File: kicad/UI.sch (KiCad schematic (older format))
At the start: 14 parts, among them Q14 DMN3065LW-7, SW2 UPLOAD, U8 PCA9632

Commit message: コンデンサを追加
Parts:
- renumbered C16 to C17
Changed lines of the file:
@@
 $EndDescr
 $Comp
-L power:GND #PWR070
+L power:GND #PWR072
 U 1 1 57CEA2EF
 P 6500 4600
-F 0 "#PWR070" H 6500 4350 50  0001 C CNN
+F 0 "#PWR072" H 6500 4350 50  0001 C CNN
 F 1 "GND" H 6500 4450 50  0000 C CNN
 F 2 "" H 6500 4600 50  0000 C CNN
@@
 	6500 4600 6500 4400
 $Comp
-L power:GND #PWR072
+L power:GND #PWR074
 U 1 1 5A1C53C4
 P 7900 4600
-F 0 "#PWR072" H 7900 4350 50  0001 C CNN
+F 0 "#PWR074" H 7900 4350 50  0001 C CNN
 F 1 "GND" H 7900 4450 50  0000 C CNN
 F 2 "" H 7900 4600 50  0000 C CNN
@@
 SDA
 $Comp
-L power:+3.3V #PWR064
+L power:+3.3V #PWR066
 U 1 1 5A202D5A
 P 4050 3150
-F 0 "#PWR064" H 4050 3000 50  0001 C CNN
+F 0 "#PWR066" H 4050 3000 50  0001 C CNN
 F 1 "+3.3V" H 4050 3290 50  0000 C CNN
 F 2 "" H 4050 3150 50  0001 C CNN
@@
 	4050 3150 4050 3250
 $Comp
-L power:GND #PWR065
+L power:GND #PWR067
 U 1 1 5A202F53
 P 4050 4650
-F 0 "#PWR065" H 4050 4400 50  0001 C CNN
+F 0 "#PWR067" H 4050 4400 50  0001 C CNN
 F 1 "GND" H 4050 4500 50  0000 C CNN
 F 2 "" H 4050 4650 50  0000 C CNN
@@
 	5050 3450 5050 3550
 $Comp
-L power:+3.3V #PWR067
+L power:+3.3V #PWR069
 U 1 1 5A204571
 P 5050 3150
-F 0 "#PWR067" H 5050 3000 50  0001 C CNN
+F 0 "#PWR069" H 5050 3000 50  0001 C CNN
 F 1 "+3.3V" H 5050 3290 50  0000 C CNN
 F 2 "" H 5050 3150 50  0001 C CNN
@@
 	4750 3450 4750 3550
 $Comp
-L power:+3.3V #PWR066
+L power:+3.3V #PWR068
 U 1 1 5A203D72
 P 4750 3150
-F 0 "#PWR066" H 4750 3000 50  0001 C CNN
+F 0 "#PWR068" H 4750 3000 50  0001 C CNN
 F 1 "+3.3V" H 4750 3290 50  0000 C CNN
 F 2 "" H 4750 3150 50  0001 C CNN
@@
 	5650 3450 5650 3550
 $Comp
-L power:+3.3V #PWR069
+L power:+3.3V #PWR071
 U 1 1 5A20460C
 P 5650 3150
-F 0 "#PWR069" H 5650 3000 50  0001 C CNN
+F 0 "#PWR071" H 5650 3000 50  0001 C CNN
 F 1 "+3.3V" H 5650 3290 50  0000 C CNN
 F 2 "" H 5650 3150 50  0001 C CNN
@@
 	5350 3450 5350 3550
 $Comp
-L power:+3.3V #PWR068
+L power:+3.3V #PWR070
 U 1 1 5A204620
 P 5350 3150
-F 0 "#PWR068" H 5350 3000 50  0001 C CNN
+F 0 "#PWR070" H 5350 3000 50  0001 C CNN
 F 1 "+3.3V" H 5350 3290 50  0000 C CNN
 F 2 "" H 5350 3150 50  0001 C CNN
@@
 	5650 4250 5650 3850
 $Comp
-L Device:C_Small C16
+L Device:C_Small C17
 U 1 1 5A2A1F42
 P 3850 3450
-F 0 "C16" H 3860 3520 50  0000 L CNN
+F 0 "C17" H 3860 3520 50  0000 L CNN
 F 1 "0.1u" H 3860 3370 50  0000 L CNN
 F 2 "Capacitors_SMD:C_0201_NoSilk" H 3850 3450 50  0001 C CNN
@@
 $EndComp
 $Comp
-L power:GND #PWR063
+L power:GND #PWR065
 U 1 1 5A2A2041
 P 3850 3550
-F 0 "#PWR063" H 3850 3300 50  0001 C CNN
+F 0 "#PWR065" H 3850 3300 50  0001 C CNN
 F 1 "GND" H 3850 3400 50  0000 C CNN
 F 2 "" H 3850 3550 50  0001 C CNN
@@
 	7500 4300 7600 4300
 $Comp
-L power:+3.3V #PWR071
+L power:+3.3V #PWR073
 U 1 1 5B6724D4
 P 7900 3400
-F 0 "#PWR071" H 7900 3250 50  0001 C CNN
+F 0 "#PWR073" H 7900 3250 50  0001 C CNN
 F 1 "+3.3V" H 7900 3540 50  0000 C CNN
 F 2 "" H 7900 3400 50  0001 C CNN

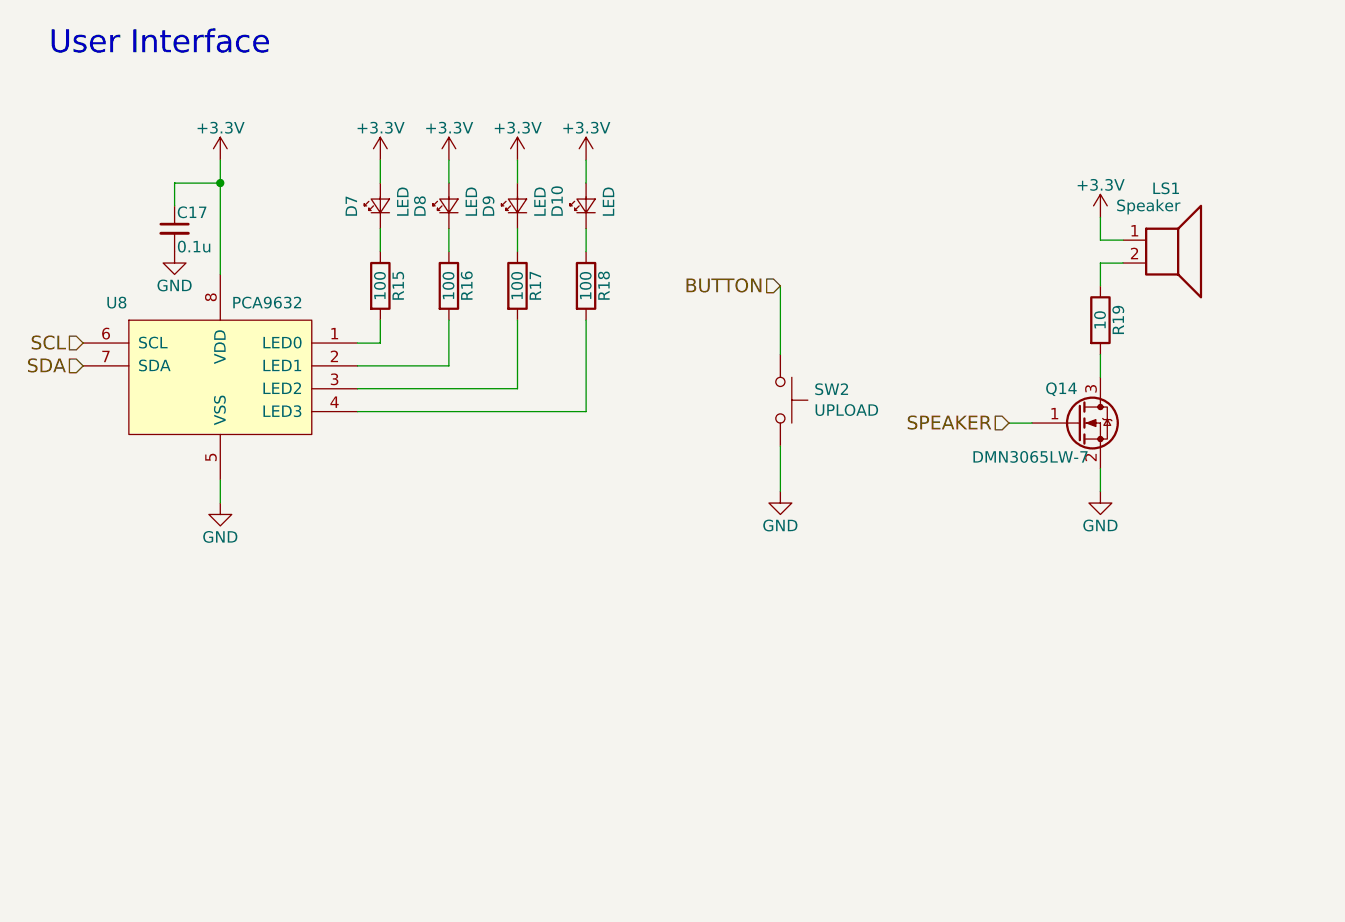
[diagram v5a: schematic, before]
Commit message: KERISEv4-5に向けて回路図を更新
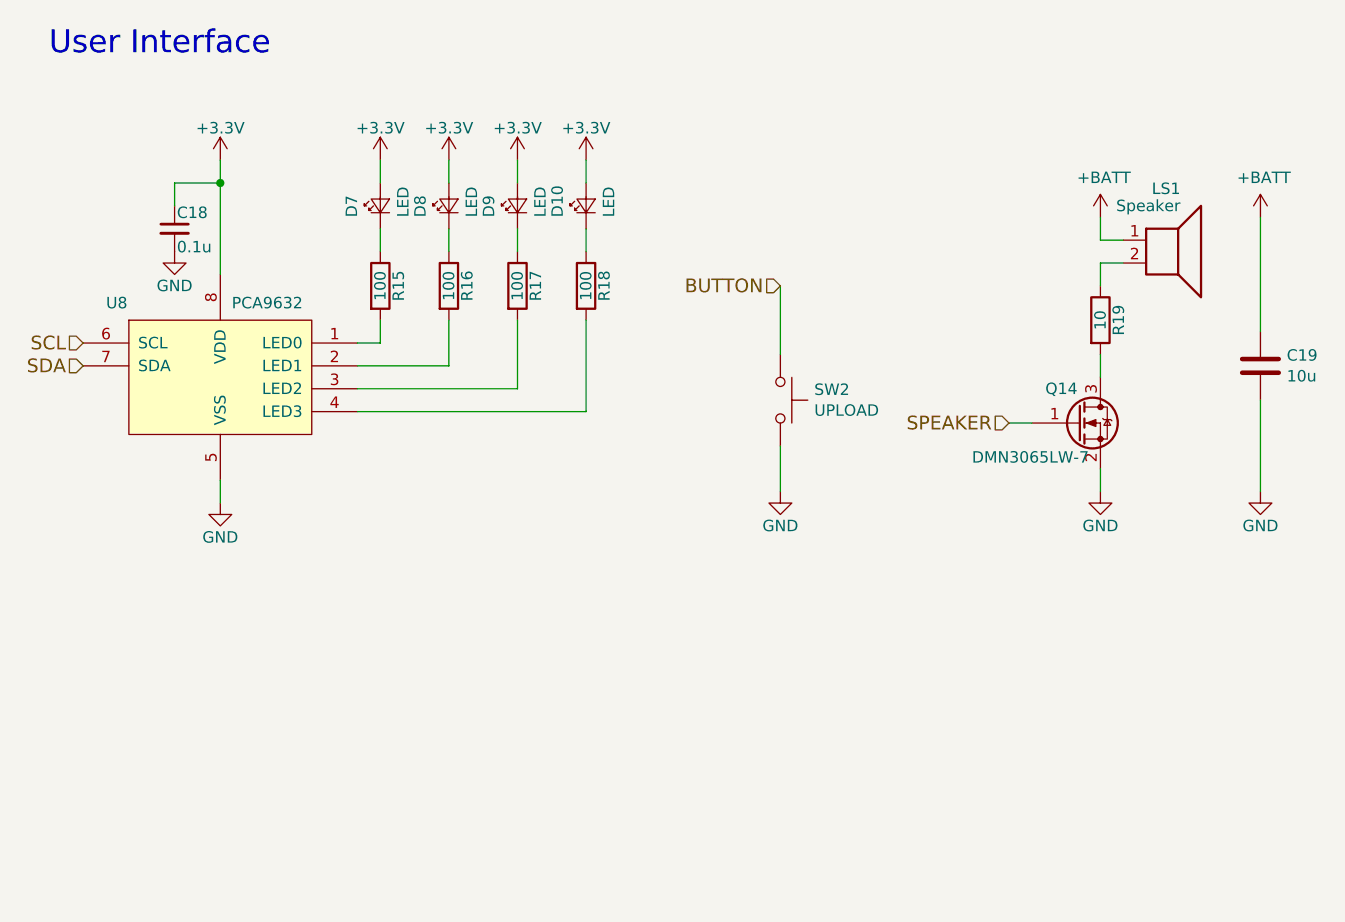
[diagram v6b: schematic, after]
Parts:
- added C19: 10u, symbol Device:C
- renumbered C17 to C18
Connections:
- net +3V3: no longer LS1.1
- net GND: now also C19.2
- new net +BATT: C19.1, LS1.1
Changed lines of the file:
@@
 $Descr A4 11693 8268
 encoding utf-8
-Sheet 14 14
+Sheet 14 15
 Title ""
 Date ""
@@
 $EndDescr
 $Comp
-L power:GND #PWR072
+L power:GND #PWR074
 U 1 1 57CEA2EF
 P 6500 4600
-F 0 "#PWR072" H 6500 4350 50  0001 C CNN
+F 0 "#PWR074" H 6500 4350 50  0001 C CNN
 F 1 "GND" H 6500 4450 50  0000 C CNN
 F 2 "" H 6500 4600 50  0000 C CNN
@@
 	6500 4600 6500 4400
 $Comp
-L power:GND #PWR074
+L power:GND #PWR076
 U 1 1 5A1C53C4
 P 7900 4600
-F 0 "#PWR074" H 7900 4350 50  0001 C CNN
+F 0 "#PWR076" H 7900 4350 50  0001 C CNN
 F 1 "GND" H 7900 4450 50  0000 C CNN
 F 2 "" H 7900 4600 50  0000 C CNN
@@
 SDA
 $Comp
-L power:+3.3V #PWR066
+L power:+3.3V #PWR068
 U 1 1 5A202D5A
 P 4050 3150
-F 0 "#PWR066" H 4050 3000 50  0001 C CNN
+F 0 "#PWR068" H 4050 3000 50  0001 C CNN
 F 1 "+3.3V" H 4050 3290 50  0000 C CNN
 F 2 "" H 4050 3150 50  0001 C CNN
@@
 	4050 3150 4050 3250
 $Comp
-L power:GND #PWR067
+L power:GND #PWR069
 U 1 1 5A202F53
 P 4050 4650
-F 0 "#PWR067" H 4050 4400 50  0001 C CNN
+F 0 "#PWR069" H 4050 4400 50  0001 C CNN
 F 1 "GND" H 4050 4500 50  0000 C CNN
 F 2 "" H 4050 4650 50  0000 C CNN
@@
 	5050 3450 5050 3550
 $Comp
-L power:+3.3V #PWR069
+L power:+3.3V #PWR071
 U 1 1 5A204571
 P 5050 3150
-F 0 "#PWR069" H 5050 3000 50  0001 C CNN
+F 0 "#PWR071" H 5050 3000 50  0001 C CNN
 F 1 "+3.3V" H 5050 3290 50  0000 C CNN
 F 2 "" H 5050 3150 50  0001 C CNN
@@
 	4750 3450 4750 3550
 $Comp
-L power:+3.3V #PWR068
+L power:+3.3V #PWR070
 U 1 1 5A203D72
 P 4750 3150
-F 0 "#PWR068" H 4750 3000 50  0001 C CNN
+F 0 "#PWR070" H 4750 3000 50  0001 C CNN
 F 1 "+3.3V" H 4750 3290 50  0000 C CNN
 F 2 "" H 4750 3150 50  0001 C CNN
@@
 	5650 3450 5650 3550
 $Comp
-L power:+3.3V #PWR071
+L power:+3.3V #PWR073
 U 1 1 5A20460C
 P 5650 3150
-F 0 "#PWR071" H 5650 3000 50  0001 C CNN
+F 0 "#PWR073" H 5650 3000 50  0001 C CNN
 F 1 "+3.3V" H 5650 3290 50  0000 C CNN
 F 2 "" H 5650 3150 50  0001 C CNN
@@
 	5350 3450 5350 3550
 $Comp
-L power:+3.3V #PWR070
+L power:+3.3V #PWR072
 U 1 1 5A204620
 P 5350 3150
-F 0 "#PWR070" H 5350 3000 50  0001 C CNN
+F 0 "#PWR072" H 5350 3000 50  0001 C CNN
 F 1 "+3.3V" H 5350 3290 50  0000 C CNN
 F 2 "" H 5350 3150 50  0001 C CNN
@@
 	5650 4250 5650 3850
 $Comp
-L Device:C_Small C17
+L Device:C_Small C18
 U 1 1 5A2A1F42
 P 3850 3450
-F 0 "C17" H 3860 3520 50  0000 L CNN
+F 0 "C18" H 3860 3520 50  0000 L CNN
 F 1 "0.1u" H 3860 3370 50  0000 L CNN
 F 2 "Capacitors_SMD:C_0201_NoSilk" H 3850 3450 50  0001 C CNN
@@
 $EndComp
 $Comp
-L power:GND #PWR065
+L power:GND #PWR067
 U 1 1 5A2A2041
 P 3850 3550
-F 0 "#PWR065" H 3850 3300 50  0001 C CNN
+F 0 "#PWR067" H 3850 3300 50  0001 C CNN
 F 1 "GND" H 3850 3400 50  0000 C CNN
 F 2 "" H 3850 3550 50  0001 C CNN
@@
 Wire Wire Line
 	7500 4300 7600 4300
-$Comp
-L power:+3.3V #PWR073
-U 1 1 5B6724D4
-P 7900 3400
-F 0 "#PWR073" H 7900 3250 50  0001 C CNN
-F 1 "+3.3V" H 7900 3540 50  0000 C CNN
-F 2 "" H 7900 3400 50  0001 C CNN
-F 3 "" H 7900 3400 50  0001 C CNN
-	1    7900 3400
-	1    0    0    -1
-$EndComp
 $Comp
 L Device:R R19
@@
 	0    1    1    0
 $EndComp
+$Comp
+L power:+BATT #PWR075
+U 1 1 5C29DB6A
+P 7900 3400
+F 0 "#PWR075" H 7900 3250 50  0001 C CNN
+F 1 "+BATT" H 7915 3573 50  0000 C CNN
+F 2 "" H 7900 3400 50  0001 C CNN
+F 3 "" H 7900 3400 50  0001 C CNN
+	1    7900 3400
+	1    0    0    -1
+$EndComp
+$Comp
+L Device:C C19
+U 1 1 5C29E0A6
+P 8600 4050
+F 0 "C19" H 8715 4096 50  0000 L CNN
+F 1 "10u" H 8715 4005 50  0000 L CNN
+F 2 "" H 8638 3900 50  0001 C CNN
+F 3 "~" H 8600 4050 50  0001 C CNN
+	1    8600 4050
+	1    0    0    -1
+$EndComp
+$Comp
+L power:+BATT #PWR077
+U 1 1 5C29E17B
+P 8600 3400
+F 0 "#PWR077" H 8600 3250 50  0001 C CNN
+F 1 "+BATT" H 8615 3573 50  0000 C CNN
+F 2 "" H 8600 3400 50  0001 C CNN
+F 3 "" H 8600 3400 50  0001 C CNN
+	1    8600 3400
+	1    0    0    -1
+$EndComp
+$Comp
+L power:GND #PWR078
+U 1 1 5C29E1A4
+P 8600 4600
+F 0 "#PWR078" H 8600 4350 50  0001 C CNN
+F 1 "GND" H 8600 4450 50  0000 C CNN
+F 2 "" H 8600 4600 50  0000 C CNN
+F 3 "" H 8600 4600 50  0000 C CNN
+	1    8600 4600
+	1    0    0    -1
+$EndComp
+Wire Wire Line
+	8600 4600 8600 4200
+Wire Wire Line
+	8600 3900 8600 3400
 $EndSCHEMATC

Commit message: フットプリントを割り当て
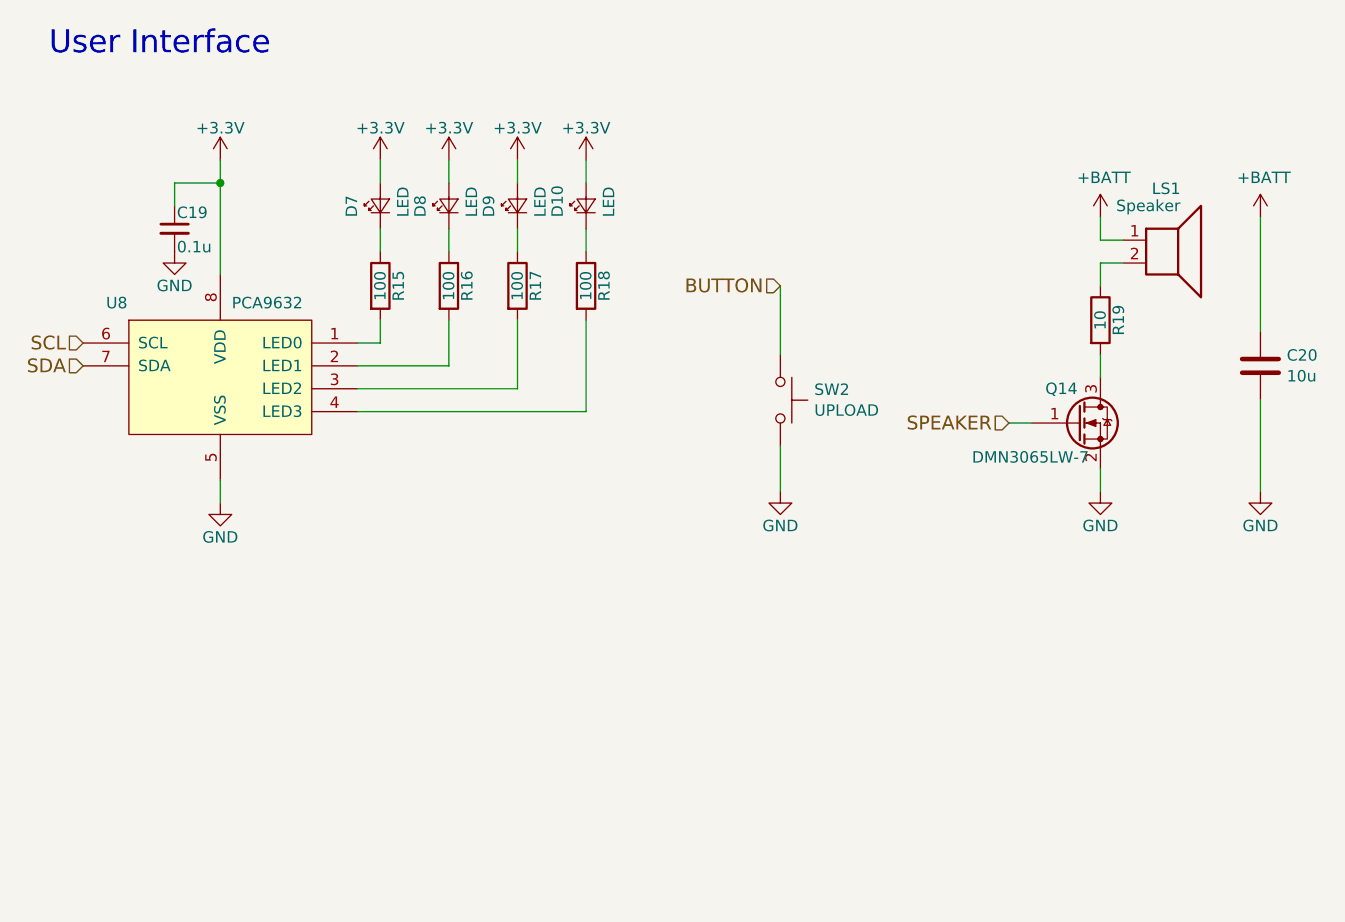
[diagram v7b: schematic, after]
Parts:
- C19: renamed from C18; footprint Capacitors_SMD:C_0201_NoSilk -> Capacitor_SMD:C_0201_0603Metric
- C20: renamed from C19; footprint (none) -> Capacitor_SMD:C_0402_1005Metric
- D10, D7, D8, D9: footprint LEDs:LED_0402 -> LED_SMD:LED_0402_1005Metric
- R15, R16, R17, R18, R19: footprint Resistors_SMD:R_0201_NoSilk -> Resistor_SMD:R_0201_0603Metric
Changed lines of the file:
@@
 $EndDescr
 $Comp
-L power:GND #PWR074
+L power:GND #PWR076
 U 1 1 57CEA2EF
 P 6500 4600
-F 0 "#PWR074" H 6500 4350 50  0001 C CNN
+F 0 "#PWR076" H 6500 4350 50  0001 C CNN
 F 1 "GND" H 6500 4450 50  0000 C CNN
 F 2 "" H 6500 4600 50  0000 C CNN
@@
 	6500 4600 6500 4400
 $Comp
-L power:GND #PWR076
+L power:GND #PWR078
 U 1 1 5A1C53C4
 P 7900 4600
-F 0 "#PWR076" H 7900 4350 50  0001 C CNN
+F 0 "#PWR078" H 7900 4350 50  0001 C CNN
 F 1 "GND" H 7900 4450 50  0000 C CNN
 F 2 "" H 7900 4600 50  0000 C CNN
@@
 SDA
 $Comp
-L power:+3.3V #PWR068
+L power:+3.3V #PWR070
 U 1 1 5A202D5A
 P 4050 3150
-F 0 "#PWR068" H 4050 3000 50  0001 C CNN
+F 0 "#PWR070" H 4050 3000 50  0001 C CNN
 F 1 "+3.3V" H 4050 3290 50  0000 C CNN
 F 2 "" H 4050 3150 50  0001 C CNN
@@
 	4050 3150 4050 3250
 $Comp
-L power:GND #PWR069
+L power:GND #PWR071
 U 1 1 5A202F53
 P 4050 4650
-F 0 "#PWR069" H 4050 4400 50  0001 C CNN
+F 0 "#PWR071" H 4050 4400 50  0001 C CNN
 F 1 "GND" H 4050 4500 50  0000 C CNN
 F 2 "" H 4050 4650 50  0000 C CNN
@@
 	5050 3450 5050 3550
 $Comp
-L power:+3.3V #PWR071
+L power:+3.3V #PWR073
 U 1 1 5A204571
 P 5050 3150
-F 0 "#PWR071" H 5050 3000 50  0001 C CNN
+F 0 "#PWR073" H 5050 3000 50  0001 C CNN
 F 1 "+3.3V" H 5050 3290 50  0000 C CNN
 F 2 "" H 5050 3150 50  0001 C CNN
@@
 F 0 "R16" V 5130 3700 50  0000 C CNN
 F 1 "100" V 5050 3700 50  0000 C CNN
-F 2 "Resistors_SMD:R_0201_NoSilk" V 4980 3700 50  0001 C CNN
+F 2 "Resistor_SMD:R_0201_0603Metric" V 4980 3700 50  0001 C CNN
 F 3 "" H 5050 3700 50  0001 C CNN
 	1    5050 3700
@@
 F 0 "D8" H 5000 3475 50  0000 L CNN
 F 1 "LED" H 5000 3250 50  0000 L CNN
-F 2 "LEDs:LED_0402" V 5050 3350 50  0001 C CNN
+F 2 "LED_SMD:LED_0402_1005Metric" V 5050 3350 50  0001 C CNN
 F 3 "" V 5050 3350 50  0001 C CNN
 	1    5050 3350
@@
 	4750 3450 4750 3550
 $Comp
-L power:+3.3V #PWR070
+L power:+3.3V #PWR072
 U 1 1 5A203D72
 P 4750 3150
-F 0 "#PWR070" H 4750 3000 50  0001 C CNN
+F 0 "#PWR072" H 4750 3000 50  0001 C CNN
 F 1 "+3.3V" H 4750 3290 50  0000 C CNN
 F 2 "" H 4750 3150 50  0001 C CNN
@@
 F 0 "R15" V 4830 3700 50  0000 C CNN
 F 1 "100" V 4750 3700 50  0000 C CNN
-F 2 "Resistors_SMD:R_0201_NoSilk" V 4680 3700 50  0001 C CNN
+F 2 "Resistor_SMD:R_0201_0603Metric" V 4680 3700 50  0001 C CNN
 F 3 "" H 4750 3700 50  0001 C CNN
 	1    4750 3700
@@
 F 0 "D7" H 4700 3475 50  0000 L CNN
 F 1 "LED" H 4700 3250 50  0000 L CNN
-F 2 "LEDs:LED_0402" V 4750 3350 50  0001 C CNN
+F 2 "LED_SMD:LED_0402_1005Metric" V 4750 3350 50  0001 C CNN
 F 3 "" V 4750 3350 50  0001 C CNN
 	1    4750 3350
@@
 	5650 3450 5650 3550
 $Comp
-L power:+3.3V #PWR073
+L power:+3.3V #PWR075
 U 1 1 5A20460C
 P 5650 3150
-F 0 "#PWR073" H 5650 3000 50  0001 C CNN
+F 0 "#PWR075" H 5650 3000 50  0001 C CNN
 F 1 "+3.3V" H 5650 3290 50  0000 C CNN
 F 2 "" H 5650 3150 50  0001 C CNN
@@
 F 0 "R18" V 5730 3700 50  0000 C CNN
 F 1 "100" V 5650 3700 50  0000 C CNN
-F 2 "Resistors_SMD:R_0201_NoSilk" V 5580 3700 50  0001 C CNN
+F 2 "Resistor_SMD:R_0201_0603Metric" V 5580 3700 50  0001 C CNN
 F 3 "" H 5650 3700 50  0001 C CNN
 	1    5650 3700
@@
 F 0 "D10" H 5600 3475 50  0000 L CNN
 F 1 "LED" H 5600 3250 50  0000 L CNN
-F 2 "LEDs:LED_0402" V 5650 3350 50  0001 C CNN
+F 2 "LED_SMD:LED_0402_1005Metric" V 5650 3350 50  0001 C CNN
 F 3 "" V 5650 3350 50  0001 C CNN
 	1    5650 3350
@@
 	5350 3450 5350 3550
 $Comp
-L power:+3.3V #PWR072
+L power:+3.3V #PWR074
 U 1 1 5A204620
 P 5350 3150
-F 0 "#PWR072" H 5350 3000 50  0001 C CNN
+F 0 "#PWR074" H 5350 3000 50  0001 C CNN
 F 1 "+3.3V" H 5350 3290 50  0000 C CNN
 F 2 "" H 5350 3150 50  0001 C CNN
@@
 F 0 "R17" V 5430 3700 50  0000 C CNN
 F 1 "100" V 5350 3700 50  0000 C CNN
-F 2 "Resistors_SMD:R_0201_NoSilk" V 5280 3700 50  0001 C CNN
+F 2 "Resistor_SMD:R_0201_0603Metric" V 5280 3700 50  0001 C CNN
 F 3 "" H 5350 3700 50  0001 C CNN
 	1    5350 3700
@@
 F 0 "D9" H 5300 3475 50  0000 L CNN
 F 1 "LED" H 5300 3250 50  0000 L CNN
-F 2 "LEDs:LED_0402" V 5350 3350 50  0001 C CNN
+F 2 "LED_SMD:LED_0402_1005Metric" V 5350 3350 50  0001 C CNN
 F 3 "" V 5350 3350 50  0001 C CNN
 	1    5350 3350
@@
 	5650 4250 5650 3850
 $Comp
-L Device:C_Small C18
+L Device:C_Small C19
 U 1 1 5A2A1F42
 P 3850 3450
-F 0 "C18" H 3860 3520 50  0000 L CNN
+F 0 "C19" H 3860 3520 50  0000 L CNN
 F 1 "0.1u" H 3860 3370 50  0000 L CNN
-F 2 "Capacitors_SMD:C_0201_NoSilk" H 3850 3450 50  0001 C CNN
+F 2 "Capacitor_SMD:C_0201_0603Metric" H 3850 3450 50  0001 C CNN
 F 3 "" H 3850 3450 50  0001 C CNN
 	1    3850 3450
@@
 $EndComp
 $Comp
-L power:GND #PWR067
+L power:GND #PWR069
 U 1 1 5A2A2041
 P 3850 3550
-F 0 "#PWR067" H 3850 3300 50  0001 C CNN
+F 0 "#PWR069" H 3850 3300 50  0001 C CNN
 F 1 "GND" H 3850 3400 50  0000 C CNN
 F 2 "" H 3850 3550 50  0001 C CNN
@@
 F 0 "R19" V 7980 3850 50  0000 C CNN
 F 1 "10" V 7900 3850 50  0000 C CNN
-F 2 "Resistors_SMD:R_0201_NoSilk" V 7830 3850 50  0001 C CNN
+F 2 "Resistor_SMD:R_0201_0603Metric" V 7830 3850 50  0001 C CNN
 F 3 "" H 7900 3850 50  0001 C CNN
 	1    7900 3850
@@
 $EndComp
 $Comp
-L power:+BATT #PWR075
+L power:+BATT #PWR077
 U 1 1 5C29DB6A
 P 7900 3400
-F 0 "#PWR075" H 7900 3250 50  0001 C CNN
+F 0 "#PWR077" H 7900 3250 50  0001 C CNN
 F 1 "+BATT" H 7915 3573 50  0000 C CNN
 F 2 "" H 7900 3400 50  0001 C CNN
@@
 $EndComp
 $Comp
-L Device:C C19
+L Device:C C20
 U 1 1 5C29E0A6
 P 8600 4050
-F 0 "C19" H 8715 4096 50  0000 L CNN
+F 0 "C20" H 8715 4096 50  0000 L CNN
 F 1 "10u" H 8715 4005 50  0000 L CNN
-F 2 "" H 8638 3900 50  0001 C CNN
+F 2 "Capacitor_SMD:C_0402_1005Metric" H 8638 3900 50  0001 C CNN
 F 3 "~" H 8600 4050 50  0001 C CNN
 	1    8600 4050
@@
 $EndComp
 $Comp
-L power:+BATT #PWR077
+L power:+BATT #PWR079
 U 1 1 5C29E17B
 P 8600 3400
-F 0 "#PWR077" H 8600 3250 50  0001 C CNN
+F 0 "#PWR079" H 8600 3250 50  0001 C CNN
 F 1 "+BATT" H 8615 3573 50  0000 C CNN
 F 2 "" H 8600 3400 50  0001 C CNN
@@
 $EndComp
 $Comp
-L power:GND #PWR078
+L power:GND #PWR080
 U 1 1 5C29E1A4
 P 8600 4600
-F 0 "#PWR078" H 8600 4350 50  0001 C CNN
+F 0 "#PWR080" H 8600 4350 50  0001 C CNN
 F 1 "GND" H 8600 4450 50  0000 C CNN
 F 2 "" H 8600 4600 50  0000 C CNN
